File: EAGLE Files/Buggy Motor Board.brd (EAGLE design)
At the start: 100 x 80 mm, 48 parts, among them CON0 M025MM, CON1 M025MM, IC4 4050D, IC5 LP298XS, X1 MICROSD, X2 5566-24, X3 5566-24

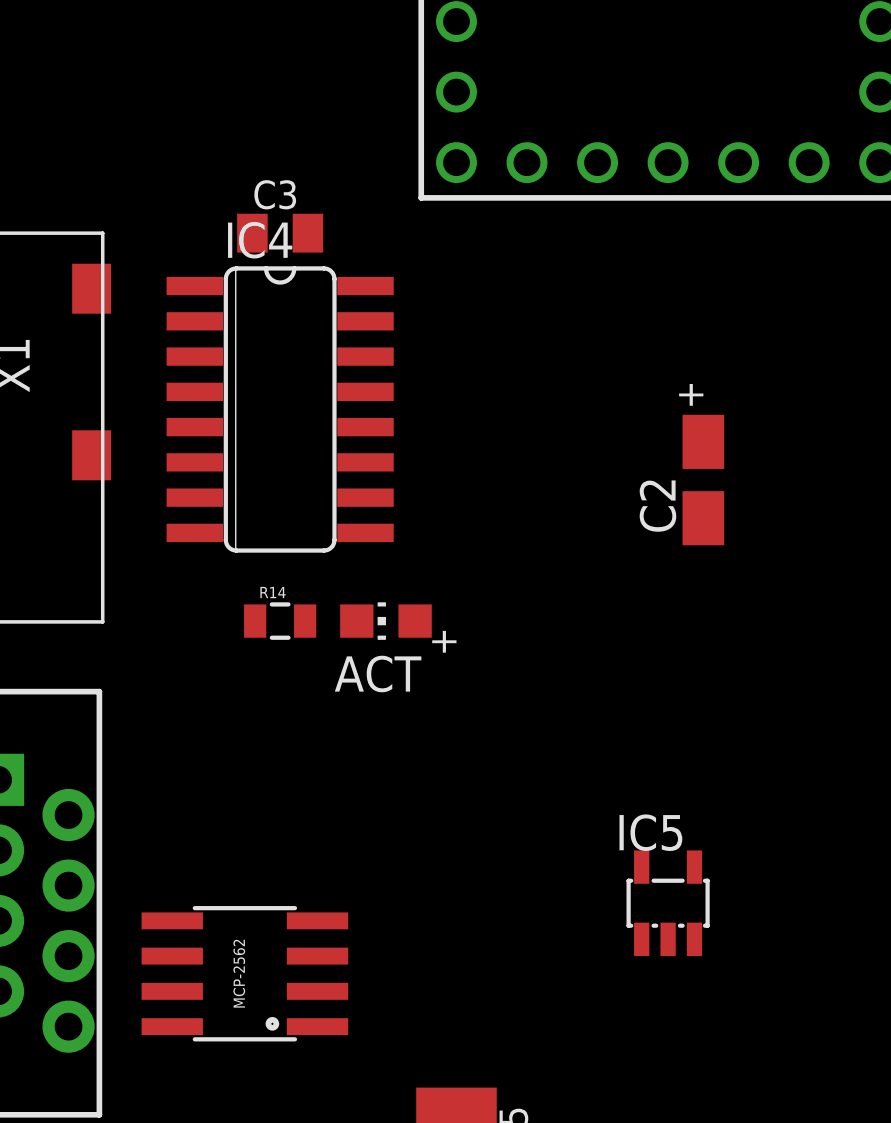
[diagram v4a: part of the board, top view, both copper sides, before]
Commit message: Remove 3v3 level shifter, add encoder inputs
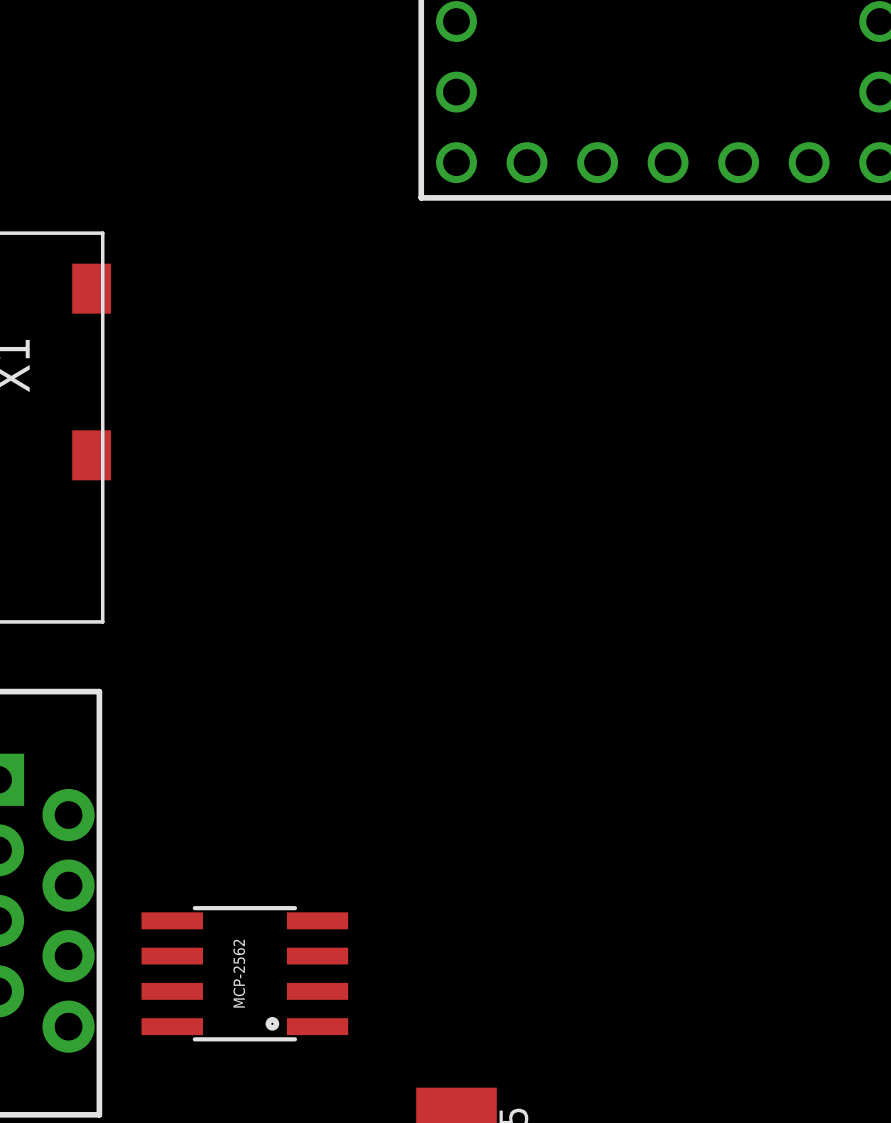
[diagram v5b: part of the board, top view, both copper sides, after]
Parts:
- removed ACT: RED, adafruit:CHIP-LED0805
- removed C2: 10uF/10V, adafruit:A/3216-18R
- removed C3: 0.1uF, adafruit:C0805K
- removed IC4: 4050D, 40xx:SO16
- removed IC5: LP298XS, adafruit:SOT23-5L
- removed R14: 1K, SparkFun-Resistors:0805
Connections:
- removed net N$17: ACT.A, IC4.10
- removed net N$18: IC4.2, X1.5
- removed net N$19: IC4.6, R14.1, X1.2
- removed net N$20: ACT.C, R14.2
- removed net N$21: IC4.4, X1.3
- new net ENC_0_A: U$10.15/A1
- new net ENC_0_B: U$10.16/A2
- new net ENC_0_Z: U$10.17/A3
- new net ENC_1_A: U$10.20/A6
- new net ENC_1_B: U$10.21/A7
- new net ENC_1_Z: U$10.22/A8
- net +3V3: no longer C2.+, C3.1, IC4.1, IC5.5
- net +5V: no longer IC5.1, IC5.3
- net GND: no longer C2.-, C3.2, IC4.11, IC4.14, IC4.8, IC5.2
- net MOSI: now also X1.3; no longer IC4.5
- net SCK: now also X1.5; no longer IC4.3, IC4.9
- net SD_CS: now also X1.2; no longer IC4.7
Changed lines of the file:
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@@
 </autorouter>
 <elements>
-<element name="ACT" library="adafruit" package="CHIP-LED0805" value="RED" x="26.67" y="29.21" rot="R90"/>
-<element name="C2" library="adafruit" package="A/3216-18R" value="10uF/10V" x="38.1" y="34.29" rot="R90"/>
-<element name="C3" library="adafruit" package="C0805K" value="0.1uF" x="22.86" y="43.18"/>
-<element name="IC4" library="40xx" package="SO16" value="4050D" x="22.86" y="36.83" rot="R270"/>
-<element name="IC5" library="adafruit" package="SOT23-5L" value="LP298XS" x="36.83" y="19.05"/>
 <element name="KSI" library="SparkFun-Connectors" package="SCREWTERMINAL-5MM-2" value="M025MM" x="67.31" y="76.2" rot="R180"/>
 <element name="PWR" library="SparkFun-Connectors" package="SCREWTERMINAL-3.5MM-2_LOCK" value="M023.5MM_LOCK" x="52.07" y="76.2" rot="R180"/>
@@
 <element name="R1" library="SparkFun-Resistors" package="0805" value="" x="63.5" y="59.69"/>
 <element name="R11" library="SparkFun-Resistors" package="0805" value="120" x="7.62" y="7.62"/>
-<element name="R14" library="SparkFun-Resistors" package="0805" value="1K" x="22.86" y="29.21"/>
 <element name="R17" library="SparkFun-Resistors" package="0805" value="" x="24.13" y="60.96" rot="R180"/>
 <element name="R2" library="SparkFun-Resistors" package="0805" value="" x="63.5" y="57.15"/>
@@
 <contactref element="X1" pad="MT2"/>
 <contactref element="X1" pad="MT1"/>
-<contactref element="IC4" pad="8"/>
-<contactref element="IC5" pad="2"/>
-<contactref element="C2" pad="-"/>
-<contactref element="C3" pad="2"/>
-<contactref element="IC4" pad="11"/>
-<contactref element="IC4" pad="14"/>
 <contactref element="U$8" pad="12"/>
 <contactref element="R17" pad="1"/>
@@
 <contactref element="U$10" pad="GND1"/>
 <contactref element="U$10" pad="GND"/>
-<wire x1="-13.02" y1="-3.81" x2="-13.02" y2="-8.89" width="0" layer="19" extent="1-1"/>
-<wire x1="-11.43" y1="2.54" x2="-13.02" y2="-3.81" width="0" layer="19" extent="1-1"/>
-<wire x1="2.07" y1="29.58" x2="-11.43" y2="2.54" width="0" layer="19" extent="1-1"/>
+<wire x1="29.21" y1="78.74" x2="52.2478" y2="76.2" width="0" layer="19" extent="1-1"/>
+<wire x1="25.03" y1="60.96" x2="29.21" y2="78.74" width="0" layer="19" extent="1-1"/>
+<wire x1="12.854" y1="59.925" x2="25.03" y2="60.96" width="0" layer="19" extent="1-1"/>
+<wire x1="36.83" y1="45.72" x2="25.03" y2="60.96" width="0" layer="19" extent="1-1"/>
+<wire x1="53.2638" y1="38.735" x2="36.83" y2="45.72" width="0" layer="19" extent="1-1"/>
+<wire x1="53.34" y1="31.75" x2="53.2638" y2="38.735" width="0" layer="19" extent="1-1"/>
+<wire x1="2.97" y1="42.78" x2="12.854" y2="59.925" width="0" layer="19" extent="1-1"/>
+<wire x1="5.47" y1="39.68" x2="2.97" y2="42.78" width="0" layer="19" extent="1-1"/>
+<wire x1="2.07" y1="29.58" x2="5.47" y2="39.68" width="0" layer="19" extent="1-1"/>
+<wire x1="15.24" y1="17.145" x2="2.07" y2="29.58" width="0" layer="19" extent="1-1"/>
+<wire x1="18.9738" y1="14.605" x2="15.24" y2="17.145" width="0" layer="19" extent="1-1"/>
+<wire x1="24.2062" y1="15.875" x2="18.9738" y2="14.605" width="0" layer="19" extent="1-1"/>
+<wire x1="29.21" y1="8.66" x2="24.2062" y2="15.875" width="0" layer="19" extent="1-1"/>
+<wire x1="32.8422" y1="3.81" x2="29.21" y2="8.66" width="0" layer="19" extent="1-1"/>
+<wire x1="44.2722" y1="3.81" x2="32.8422" y2="3.81" width="0" layer="19" extent="1-1"/>
+<wire x1="-11.43" y1="2.54" x2="2.07" y2="29.58" width="0" layer="19" extent="1-1"/>
+<wire x1="-13.02" y1="-3.81" x2="-11.43" y2="2.54" width="0" layer="19" extent="1-1"/>
+<wire x1="-13.02" y1="-8.89" x2="-13.02" y2="-3.81" width="0" layer="19" extent="1-1"/>
 </signal>
 <signal name="MODE1">
@@
 </signal>
 <signal name="+5V">
-<contactref element="IC5" pad="1"/>
-<contactref element="IC5" pad="3"/>
 <contactref element="U$9" pad="1"/>
 <contactref element="C5" pad="1"/>
@@
 <wire x1="20.166" y1="67.075" x2="44.45" y2="78.74" width="0" layer="19" extent="1-1"/>
 <wire x1="50.8" y1="31.75" x2="20.166" y2="67.075" width="0" layer="19" extent="1-1"/>
-<wire x1="37.78" y1="17.75" x2="50.8" y2="31.75" width="0" layer="19" extent="1-1"/>
-<wire x1="35.88" y1="17.75" x2="37.78" y2="17.75" width="0" layer="19" extent="1-1"/>
-<wire x1="29.21" y1="11.66" x2="35.88" y2="17.75" width="0" layer="19" extent="1-1"/>
+<wire x1="29.21" y1="11.66" x2="50.8" y2="31.75" width="0" layer="19" extent="1-1"/>
 <wire x1="24.2062" y1="17.145" x2="29.21" y2="11.66" width="0" layer="19" extent="1-1"/>
 <wire x1="-8.89" y1="2.54" x2="24.2062" y2="17.145" width="0" layer="19" extent="1-1"/>
@@
 </signal>
 <signal name="MOSI">
-<contactref element="IC4" pad="5"/>
 <contactref element="U$10" pad="11"/>
-<wire x1="19.7866" y1="36.195" x2="29.21" y2="48.26" width="0" layer="19" extent="1-1"/>
+<contactref element="X1" pad="3"/>
+<wire x1="5.87" y1="36.38" x2="29.21" y2="48.26" width="0" layer="19" extent="1-1"/>
 </signal>
 <signal name="SCL">
@@
 <wire x1="8.52" y1="7.62" x2="11.43" y2="7.62" width="0" layer="19" extent="1-1"/>
 </signal>
-<signal name="N$17">
-<contactref element="ACT" pad="A"/>
-<contactref element="IC4" pad="10"/>
-<wire x1="27.72" y1="29.21" x2="25.9334" y2="33.655" width="0" layer="19" extent="1-1"/>
-</signal>
-<signal name="N$18">
-<contactref element="IC4" pad="2"/>
-<contactref element="X1" pad="5"/>
-<wire x1="5.87" y1="38.58" x2="19.7866" y2="40.005" width="0" layer="19" extent="1-1"/>
-</signal>
-<signal name="N$19">
-<contactref element="X1" pad="2"/>
-<contactref element="R14" pad="1"/>
-<contactref element="IC4" pad="6"/>
-<wire x1="21.96" y1="29.21" x2="19.7866" y2="34.925" width="0" layer="19" extent="1-1"/>
-<wire x1="6.27" y1="35.28" x2="19.7866" y2="34.925" width="0" layer="19" extent="1-1"/>
-</signal>
 <signal name="+3V3">
 <contactref element="X1" pad="4"/>
-<contactref element="IC4" pad="1"/>
-<contactref element="IC5" pad="5"/>
-<contactref element="C2" pad="+"/>
-<contactref element="C3" pad="1"/>
 <contactref element="R15" pad="2"/>
 <contactref element="R16" pad="2"/>
@@
 <wire x1="41.91" y1="71.12" x2="44.45" y2="73.66" width="0" layer="19" extent="1-1"/>
 <wire x1="34.29" y1="45.72" x2="41.91" y2="71.12" width="0" layer="19" extent="1-1"/>
-<wire x1="38.1" y1="35.665" x2="34.29" y2="45.72" width="0" layer="19" extent="1-1"/>
-<wire x1="48.63" y1="39.37" x2="38.1" y2="35.665" width="0" layer="19" extent="1-1"/>
-<wire x1="48.63" y1="41.91" x2="48.63" y2="39.37" width="0" layer="19" extent="1-1"/>
+<wire x1="48.63" y1="41.91" x2="34.29" y2="45.72" width="0" layer="19" extent="1-1"/>
+<wire x1="48.63" y1="39.37" x2="48.63" y2="41.91" width="0" layer="19" extent="1-1"/>
 <wire x1="53.2638" y1="42.545" x2="48.63" y2="41.91" width="0" layer="19" extent="1-1"/>
-<wire x1="21.86" y1="43.18" x2="34.29" y2="45.72" width="0" layer="19" extent="1-1"/>
-<wire x1="19.7866" y1="41.275" x2="21.86" y2="43.18" width="0" layer="19" extent="1-1"/>
-<wire x1="5.47" y1="37.48" x2="19.7866" y2="41.275" width="0" layer="19" extent="1-1"/>
-<wire x1="35.88" y1="20.35" x2="38.1" y2="35.665" width="0" layer="19" extent="1-1"/>
-<wire x1="18.9738" y1="18.415" x2="35.88" y2="20.35" width="0" layer="19" extent="1-1"/>
+<wire x1="5.47" y1="37.48" x2="34.29" y2="45.72" width="0" layer="19" extent="1-1"/>
+<wire x1="18.9738" y1="18.415" x2="5.47" y2="37.48" width="0" layer="19" extent="1-1"/>
 </signal>
 <signal name="CD">
 <contactref element="X1" pad="CD1"/>
-</signal>
-<signal name="N$20">
-<contactref element="ACT" pad="C"/>
-<contactref element="R14" pad="2"/>
-<wire x1="23.76" y1="29.21" x2="25.62" y2="29.21" width="0" layer="19" extent="1-1"/>
-</signal>
-<signal name="N$21">
-<contactref element="X1" pad="3"/>
-<contactref element="IC4" pad="4"/>
-<wire x1="5.87" y1="36.38" x2="19.7866" y2="37.465" width="0" layer="19" extent="1-1"/>
 </signal>
 <signal name="AMUX_IN">
@@
 </signal>
 <signal name="SD_CS">
-<contactref element="IC4" pad="7"/>
 <contactref element="U$10" pad="5"/>
-<wire x1="19.7866" y1="33.655" x2="29.21" y2="63.5" width="0" layer="19" extent="1-1"/>
+<contactref element="X1" pad="2"/>
+<wire x1="6.27" y1="35.28" x2="29.21" y2="63.5" width="0" layer="19" extent="1-1"/>
 </signal>
 <signal name="AMUX_EN">
@@
 <signal name="SCK">
 <contactref element="U$10" pad="13"/>
-<contactref element="IC4" pad="3"/>
-<contactref element="IC4" pad="9"/>
-<wire x1="25.9334" y1="32.385" x2="44.45" y2="45.72" width="0" layer="19" extent="1-1"/>
-<wire x1="19.7866" y1="38.735" x2="25.9334" y2="32.385" width="0" layer="19" extent="1-1"/>
+<contactref element="X1" pad="5"/>
+<wire x1="5.87" y1="38.58" x2="44.45" y2="45.72" width="0" layer="19" extent="1-1"/>
+</signal>
+<signal name="ENC_0_A">
+<contactref element="U$10" pad="15/A1"/>
+</signal>
+<signal name="ENC_0_B">
+<contactref element="U$10" pad="16/A2"/>
+</signal>
+<signal name="ENC_0_Z">
+<contactref element="U$10" pad="17/A3"/>
+</signal>
+<signal name="ENC_1_A">
+<contactref element="U$10" pad="20/A6"/>
+</signal>
+<signal name="ENC_1_B">
+<contactref element="U$10" pad="21/A7"/>
+</signal>
+<signal name="ENC_1_Z">
+<contactref element="U$10" pad="22/A8"/>
 </signal>
 </signals>
